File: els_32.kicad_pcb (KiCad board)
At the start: 2 copper layers, 52 parts, among them J1 HR911105A, J2 JST-XH, J3 JST-XH, J4 Conn_01x03_Female, J5 WAGO, Q1 2N7002, Q2 Q_PMOS_DGS, U1 LAN8720A, U2 ESP32-WROOM-E, U3 MP2307, U4 LM3940

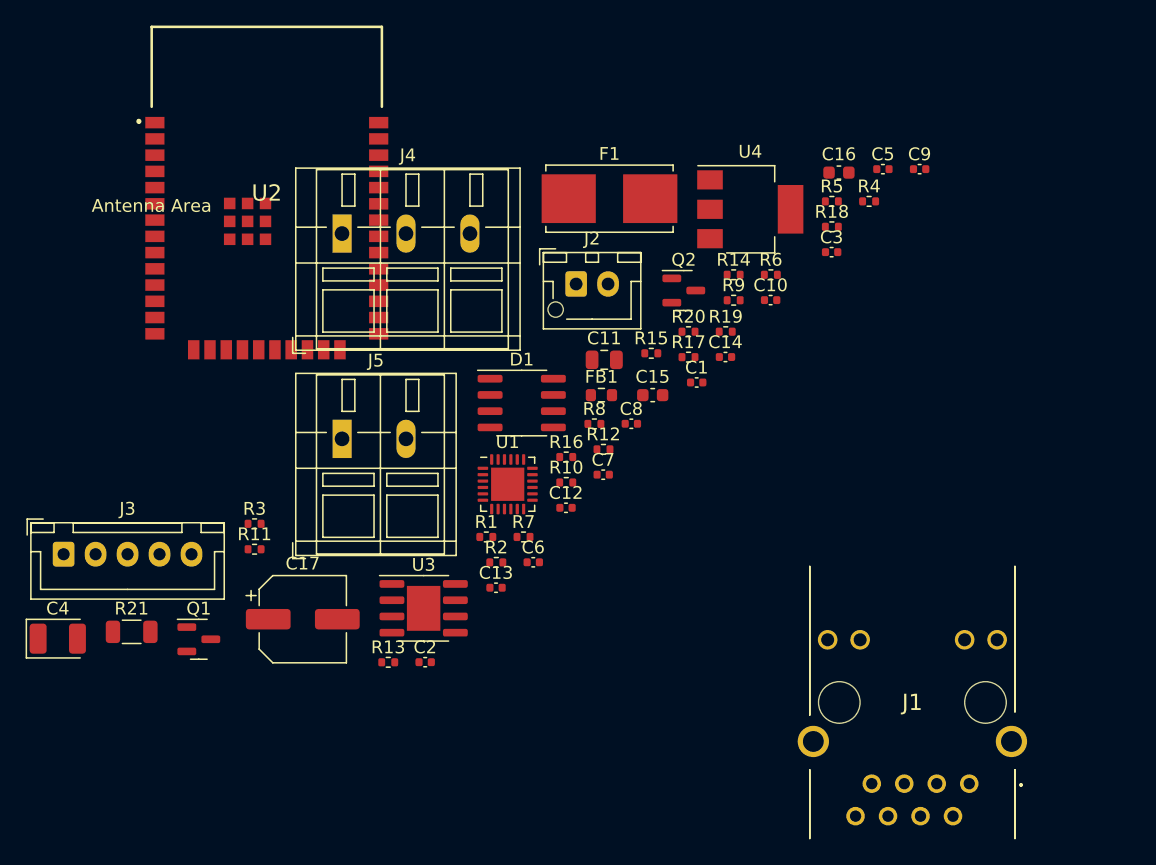
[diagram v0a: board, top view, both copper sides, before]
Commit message: Update schematic: v0.2
- use TPS54321 for VDC -> 3.3V
- use 5.6 zener for level-shifting
- cleanup
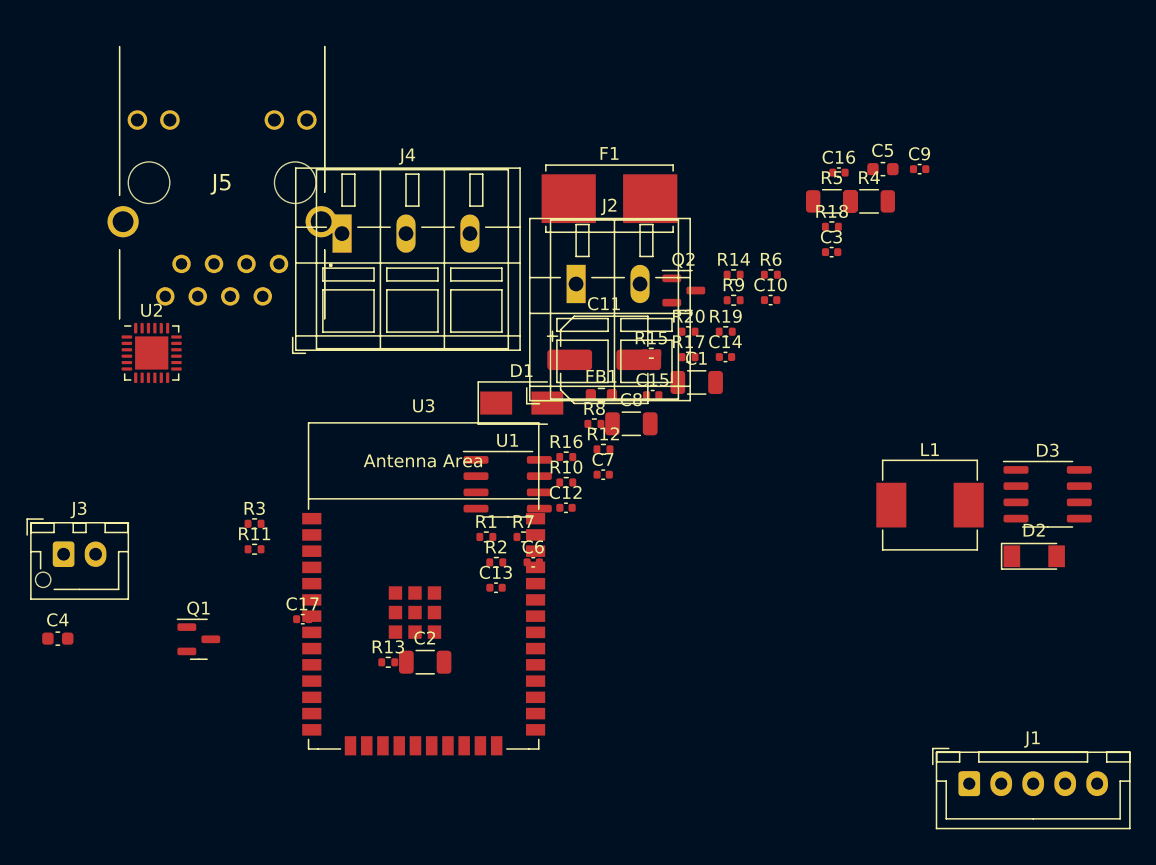
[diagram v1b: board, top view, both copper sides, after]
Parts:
- removed R21: 0, Resistor_SMD:R_1206_3216Metric
- removed U4: LM3940, Package_TO_SOT_SMD:SOT-223-3_TabPin2
- added D2: ZMMxx, Diode_SMD:D_MiniMELF, F.Cu at (210.8, 88.9)
- added D3: CDNBS08-SLVU2.8-4, Package_SO:SOIC-8_3.9x4.9mm_P1.27mm, F.Cu at (211.9, 84.0)
- added L1: 47u, Inductor_SMD:L_Sunlord_MWSA06xxS, F.Cu at (202.7, 84.9)
- C1, C2: value 10nF -> 10u; footprint Capacitor_SMD:C_0402_1005Metric -> Capacitor_SMD:C_1206_3216Metric
- C10, C7: value 100nF -> 100n
- C11: value 22u/25V -> 220u; footprint Capacitor_SMD:C_0805_2012Metric -> Capacitor_SMD:CP_Elec_6.3x7.7
- C12: value 100nF -> 22n
- C13: value 3.9nF -> 1u
- C14: value 10nF -> 470p
- C15: value 22uF 6.3V -> 100n; footprint Capacitor_SMD:C_0603_1608Metric -> Capacitor_SMD:C_0402_1005Metric
- C16: value 22uF 6.3V -> 10n; footprint Capacitor_SMD:C_0603_1608Metric -> Capacitor_SMD:C_0402_1005Metric
- C17: value 220u -> 10n; footprint Capacitor_SMD:CP_Elec_6.3x7.7 -> Capacitor_SMD:C_0402_1005Metric
- C3: value 4.7uF -> 10n
- C4: value 22uF -> 10p; footprint Capacitor_Tantalum_SMD:CP_EIA-3528-21_Kemet-B -> Capacitor_SMD:C_0603_1608Metric
- C5: value 100nF -> 15n; footprint Capacitor_SMD:C_0402_1005Metric -> Capacitor_SMD:C_0603_1608Metric
- C6: value 22nF -> 10n
- C8: value 1uF -> 47u; footprint Capacitor_SMD:C_0402_1005Metric -> Capacitor_SMD:C_1206_3216Metric
- C9: value 470pF -> 4.7uF
- D1: value CDNBS08-SLVU2.8-4 -> SS14; footprint Package_SO:SOIC-8_3.9x4.9mm_P1.27mm -> Diode_SMD:D_SMA
- J1: value HR911105A -> JST-XH; footprint els_32-libs:HR911105A -> Connector_JST:JST_XH_B5B-XH-A_1x05_P2.50mm_Vertical
- J2: value JST-XH -> WAGO; footprint Connector_JST:JST_XH_B2B-XH-AM_1x02_P2.50mm_Vertical -> TerminalBlock_WAGO:TerminalBlock_WAGO_236-102_1x02_P5.00mm_45Degree
- J3: footprint Connector_JST:JST_XH_B5B-XH-A_1x05_P2.50mm_Vertical -> Connector_JST:JST_XH_B2B-XH-AM_1x02_P2.50mm_Vertical
- J5: value WAGO -> HR911105A; footprint TerminalBlock_WAGO:TerminalBlock_WAGO_236-102_1x02_P5.00mm_45Degree -> els_32-libs:HR911105A
- Q1: value 2N7002 -> Q_PMOS_DGS
- Q2: value Q_PMOS_DGS -> 2N7002
- R1: value 330R -> 4.7K
- R10: value 49.9R -> 10
- R11: value 12.1K / 1% -> 10
- R13: value 1.5K -> 10
- R14: value 10K -> 1.5K
- R15: value 100K -> 12.1K / 1%
- R16: value 6.8K -> 49.9
- R17: value 10K/1% -> 49.9
- R18: value 44.2K -> 49.9
- R19: value 10K -> 49.9
- R2: value 330R -> 10K
- R20: value 10K -> 33
- R3: value 33 -> 3.3K
- R4: value 10 -> 0; footprint Resistor_SMD:R_0402_1005Metric -> Resistor_SMD:R_1206_3216Metric
- R5: value 10 -> 2K; footprint Resistor_SMD:R_0402_1005Metric -> Resistor_SMD:R_1206_3216Metric
- R6: value 10 -> 10K
- R7, R8: value 49.9R -> 330
- R9: value 49.9R -> 10K
- U1: value LAN8720A -> TPS54233; footprint Package_DFN_QFN:QFN-24-1EP_4x4mm_P0.5mm_EP2.6x2.6mm -> Package_SO:SOIC-8_3.9x4.9mm_P1.27mm
- U2: value ESP32-WROOM-E -> LAN8720A; footprint els_32-libs:ESP32WROOM32E -> Package_DFN_QFN:QFN-24-1EP_4x4mm_P0.5mm_EP2.6x2.6mm
- U3: value MP2307 -> ESP32-WROOM-32E; footprint Package_SO:SOIC-8-1EP_3.9x4.9mm_P1.27mm_EP2.62x3.51mm -> els_32-libs:ESP32-WROOM-32E
- moved J5 14.5 mm to (151.8, 66.0)
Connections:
- C1 pad 1: VDDA -> GND
- C1 pad 2: GND -> +VDC
- C12 pad 1: Net-(C12-Pad1) -> GND
- C12 pad 2: GND -> VDDA
- C13 pad 1: Net-(C13-Pad1) -> VDD
- C13 pad 2: Net-(C13-Pad2) -> GND
- C14 pad 1: Net-(C14-Pad1) -> VDD
- C14 pad 2: Net-(C14-Pad2) -> GND
- C15 pad 1: +5V -> +3.3V
- C16 pad 1: +5V -> VDDA
- C17 pad 1: +VDC -> VDDA
- C2 pad 1: VDDA -> +VDC
- C3 pad 2: VDDA -> +VDC
- C4 pad 1: +3.3V -> GND
- C4 pad 2: GND -> Net-(C4-Pad2)
- C5 pad 1: +3.3V -> Net-(C5-Pad1)
- C6 pad 2: VDDA -> Net-(C6-Pad2)
- C7 pad 1: +3.3V -> Net-(C7-Pad1)
- C7 pad 2: GND -> Net-(C7-Pad2)
- C8 pad 2: VDD -> +3.3V
- C9 pad 2: VDD -> VDDA
- D1 pad 1: /TXP -> Net-(C7-Pad2)
- D1 pad 2: /TXN -> GND
- J1 pad 1: /TXP -> GND
- J1 pad 2: /TXN -> /~{BOOT}
- J1 pad 3: /RXP -> /ENABLE
- J1 pad 4: VDDA -> /TXD
- J1 pad 5: VDDA -> /RXD
- J2 pad 2: +3.3V -> Net-(F1-Pad2)
- J3 pad 2: /~{BOOT} -> +3.3V
- J5 pad 1: GND -> /TXP
- J5 pad 2: Net-(F1-Pad2) -> /TXN
- Q1 pad 1: +3.3V -> GND
- Q1 pad 2: /~{LED_DATA33} -> Net-(F1-Pad1)
- Q1 pad 3: /LED_DATA5 -> +VDC
- Q2 pad 1: GND -> +3.3V
- Q2 pad 2: Net-(F1-Pad1) -> /LED_DATA33
- Q2 pad 3: +VDC -> /LED_DATA5
- R1 pad 1: Net-(J1-Pad9) -> Net-(C4-Pad2)
- R1 pad 2: /LED_G -> Net-(C5-Pad1)
- R10 pad 1: Net-(R10-Pad1) -> /RXD0
- R10 pad 2: VDDA -> Net-(R10-Pad2)
- R11 pad 1: Net-(U1-Pad24) -> /RXD1
- R11 pad 2: GND -> Net-(R11-Pad2)
- R12 pad 1: /CRS_DV -> unconnected-(R12-Pad1)
- R12 pad 2: Net-(U1-Pad11) -> Net-(R12-Pad2)
- R13 pad 1: /MDIO -> /CRS_DV
- R13 pad 2: VDD -> Net-(R13-Pad2)
- R14 pad 1: +3.3V -> /MDIO
- R14 pad 2: /ENABLE -> VDD
- R15 pad 1: +VDC -> Net-(R15-Pad1)
- R15 pad 2: Net-(R15-Pad2) -> GND
- R16 pad 1: Net-(C13-Pad2) -> Net-(D3-Pad8)
- R16 pad 2: GND -> VDDA
- R17 pad 1: Net-(R17-Pad1) -> Net-(D3-Pad7)
- R17 pad 2: GND -> VDDA
- R18 pad 1: +5V -> Net-(D3-Pad6)
- R18 pad 2: Net-(R17-Pad1) -> VDDA
- R19 pad 1: /~{LED_DATA33} -> Net-(D3-Pad5)
- R19 pad 2: +3.3V -> VDDA
- R2 pad 1: /LED_Y -> Net-(C7-Pad2)
- R2 pad 2: Net-(J1-Pad11) -> Net-(R2-Pad2)
- R20 pad 1: /LED_DATA5 -> Net-(R20-Pad1)
- R20 pad 2: +5V -> /REF_CLK
- R3 pad 1: Net-(R3-Pad1) -> Net-(R2-Pad2)
- R3 pad 2: /REF_CLK -> GND
- R4 pad 1: /RXD1 -> VDD
- R4 pad 2: Net-(U1-Pad7) -> +3.3V
- R5 pad 1: /RXD0 -> +VDC
- R5 pad 2: Net-(U1-Pad8) -> /LED_DATA5
- R6 pad 1: unconnected-(R6-Pad1) -> +3.3V
- R6 pad 2: Net-(U1-Pad10) -> /ENABLE
- R7 pad 1: Net-(U1-Pad21) -> Net-(J5-Pad9)
- R7 pad 2: VDDA -> /LED_G
- R8 pad 1: Net-(R8-Pad1) -> /LED_Y
- R8 pad 2: VDDA -> Net-(J5-Pad11)
- R9 pad 1: Net-(R9-Pad1) -> /LED_DATA33
- R9 pad 2: VDDA -> +3.3V
- U1 pad 1: VDDA -> Net-(C7-Pad1)
- U1 pad 2: /LED_Y -> +VDC
- U1 pad 3: /LED_G -> unconnected-(U1-Pad3)
- U1 pad 4: unconnected-(U1-Pad4) -> Net-(C6-Pad2)
- U1 pad 5: /REF_CLK -> Net-(R2-Pad2)
- U1 pad 6: VDD -> Net-(C4-Pad2)
- U1 pad 7: Net-(U1-Pad7) -> GND
- U1 pad 8: Net-(U1-Pad8) -> Net-(C7-Pad2)
- U2 pad 1: GND -> VDDA
- U2 pad 10: /RXD0 -> Net-(R12-Pad2)
- U2 pad 11: /RXD1 -> Net-(R13-Pad2)
- U2 pad 12: /CRS_DV -> /MDIO
- U2 pad 13: unconnected-(U2-Pad13) -> /MDC
- U2 pad 15: GND -> /~{RST}
- U2 pad 16: unconnected-(U2-Pad16) -> /TXEN
- U2 pad 17: unconnected-(U2-Pad17) -> /TXD0
- U2 pad 18: unconnected-(U2-Pad18) -> /TXD1
- U2 pad 19: unconnected-(U2-Pad19) -> VDDA
- U2 pad 2: +3.3V -> /LED_Y
- U2 pad 20: unconnected-(U2-Pad20) -> Net-(D3-Pad7)
- U2 pad 21: unconnected-(U2-Pad21) -> Net-(D3-Pad8)
- U2 pad 22: unconnected-(U2-Pad22) -> Net-(D3-Pad5)
- U2 pad 23: unconnected-(U2-Pad23) -> Net-(D3-Pad6)
- U2 pad 24: unconnected-(U2-Pad24) -> Net-(R15-Pad1)
- U2 pad 25: /~{BOOT} -> GND
- U2 pad 3: /ENABLE -> /LED_G
- U2 pad 5: unconnected-(U2-Pad5) -> /REF_CLK
- U2 pad 6: unconnected-(U2-Pad6) -> VDD
- U2 pad 7: unconnected-(U2-Pad7) -> Net-(R11-Pad2)
- U2 pad 8: unconnected-(U2-Pad8) -> Net-(R10-Pad2)
- U2 pad 9: unconnected-(U2-Pad9) -> +3.3V
- U3 pad 1: Net-(C14-Pad2) -> GND
- U3 pad 2: +VDC -> +3.3V
- U3 pad 3: Net-(C14-Pad1) -> /ENABLE
- U3 pad 4: GND -> unconnected-(U3-Pad4)
- U3 pad 5: Net-(R17-Pad1) -> unconnected-(U3-Pad5)
- U3 pad 6: Net-(C13-Pad1) -> unconnected-(U3-Pad6)
- U3 pad 7: Net-(R15-Pad2) -> unconnected-(U3-Pad7)
- U3 pad 8: Net-(C12-Pad1) -> unconnected-(U3-Pad8)
- U3 pad 9: (no net) -> unconnected-(U3-Pad9)
